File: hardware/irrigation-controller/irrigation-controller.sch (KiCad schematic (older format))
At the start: 80 parts, among them J1 RS485, J10 I2C_2, J11 IO, J12 RELAY_2, J13 RELAY_3B, J14 RELAY_4B, J15 FLOW, J2 I2C_1, J3 ATMEGA ICSP, J4 ATMEGA UART, J5 RF Module, J6 PWR, J7 RELAY_1, J8 RELAY_3A, J9 RELAY_4A, K1 UA2-5NU, K2 UA2-5NU, Q1 MMBT3904, Q2 MMBT3904, Q3 2N7002, Q4 2N7002, Q5 2N7002, Q6 2N7002, SW1 SPST, SW2 SPST, U1 AQY280EH, U2 ATmega328P-AU, U3 AQY280EH, U4 TPS54331DR, U5 TPS54331DR, U6 MAX485, Y1 8MHz

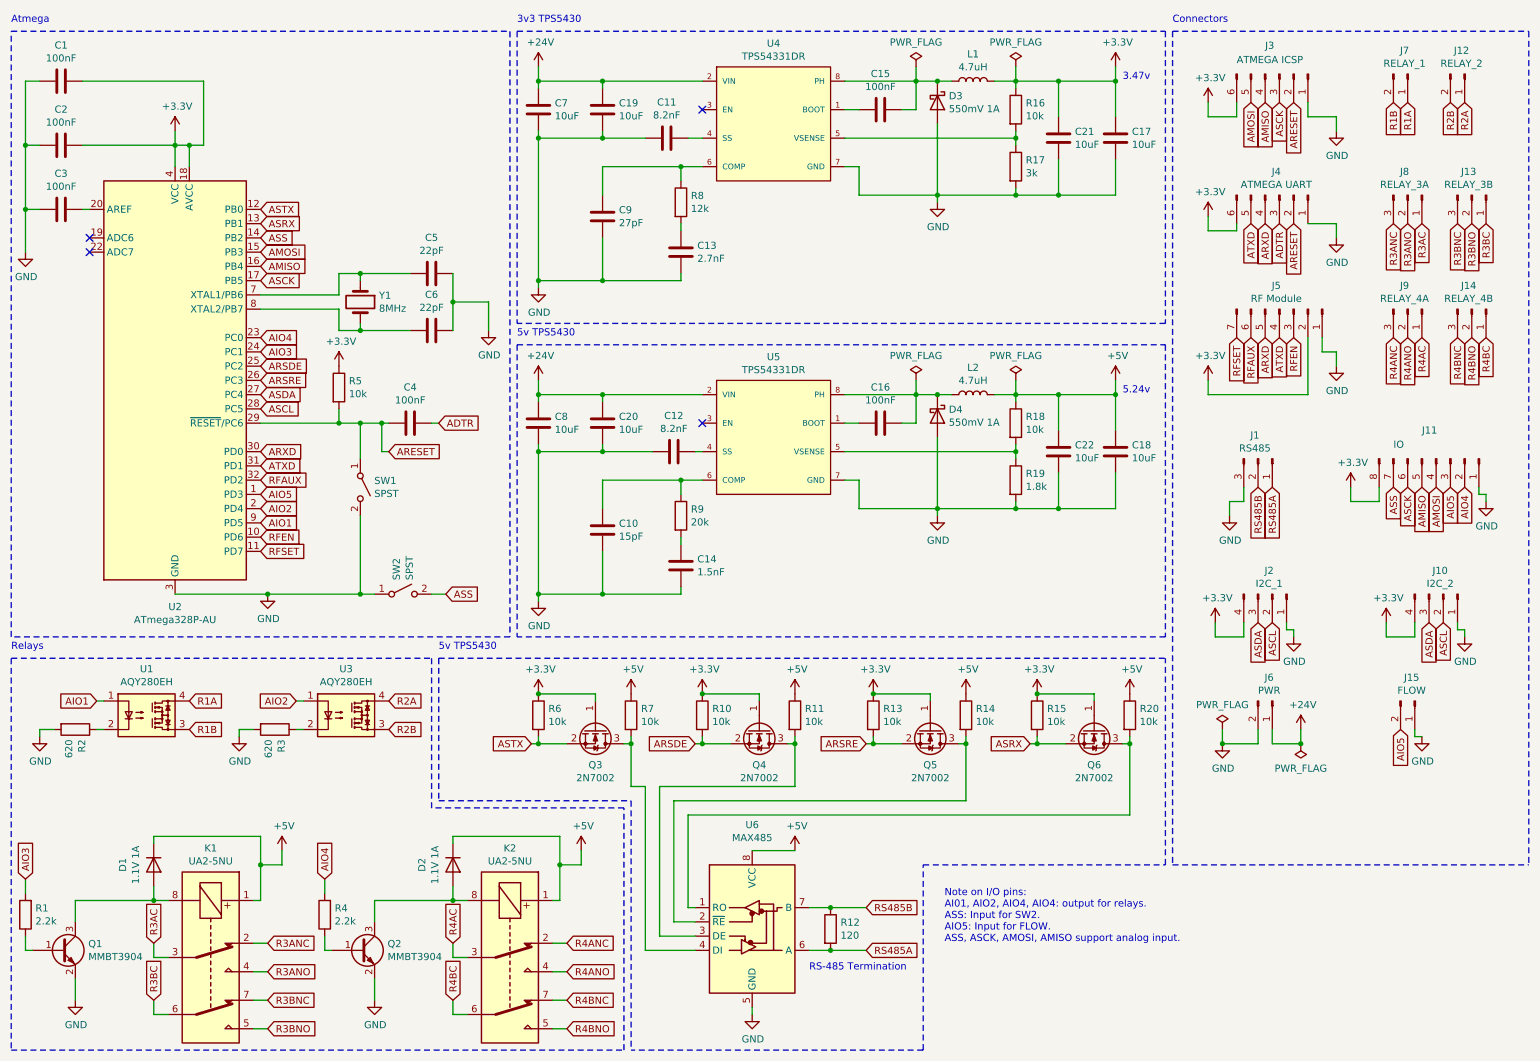
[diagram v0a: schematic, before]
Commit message: Controller board layout wip
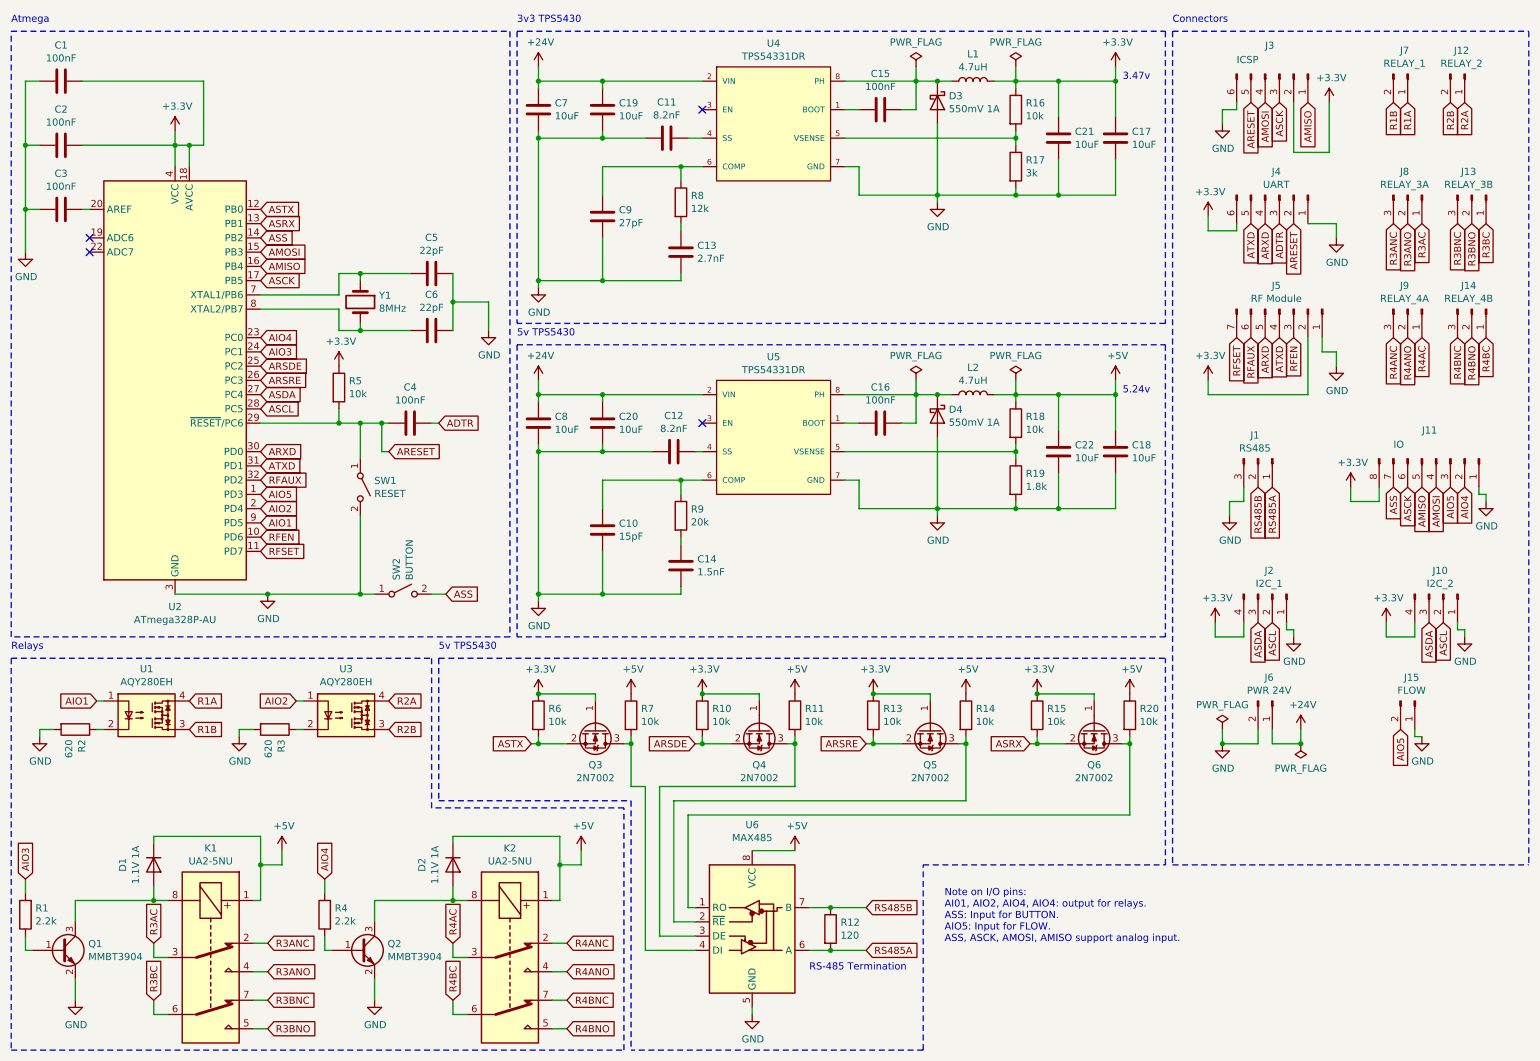
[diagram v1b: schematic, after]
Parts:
- J3: value ATMEGA ICSP -> ICSP
- J4: value ATMEGA UART -> UART
- J6: value PWR -> PWR 24V
- SW1: value SPST -> RESET
- SW2: value SPST -> BUTTON
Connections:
- net +3V3: now also J3.2 (Pin_2); no longer J3.6 (Pin_6)
- net AMISO: now also J3.1 (Pin_1); no longer J3.4 (Pin_4)
- net AMOSI: now also J3.4 (Pin_4); no longer J3.5 (Pin_5)
- net ARESET: now also J3.5 (Pin_5); no longer J3.2 (Pin_2)
- net GND: now also J3.6 (Pin_6); no longer J3.1 (Pin_1)
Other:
- note added: "Note on I/O pins:\nAI01, AIO2, AIO4, AIO4: output for relays.\nASS: Input for BUTTON.\nAIO5: Input for FLOW.\nASS, ASCK, AMOSI, AMISO support analog input."
- note removed: "Note on I/O pins:\nAI01, AIO2, AIO4, AIO4: output for relays.\nASS: Input for SW2.\nAIO5: Input for FLOW.\nASS, ASCK, AMOSI, AMISO support analog input."
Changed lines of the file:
@@
 P 2950 3800
 F 0 "SW1" V 2904 3898 50  0000 L CNN
-F 1 "SPST" V 2995 3898 50  0000 L CNN
+F 1 "RESET" V 2995 3898 50  0000 L CNN
 F 2 "lib:SW_SPST_THT_5.0mm" H 2950 3800 50  0001 C CNN
 F 3 "https://www.farnell.com/datasheets/3176355.pdf" H 2950 3800 50  0001 C CNN
@@
 Wire Wire Line
 	9600 3150 8900 3150
-Text GLabel 9200 1100 3    50   Input ~ 0
+Text GLabel 9300 1100 3    50   Input ~ 0
 AMOSI
-Text GLabel 9300 1100 3    50   Input ~ 0
+Text GLabel 9600 1100 3    50   Input ~ 0
 AMISO
 Text GLabel 9400 1100 3    50   Input ~ 0
@@
 Text GLabel 9200 1950 3    50   Input ~ 0
 ATXD
-Text GLabel 9500 1100 3    50   Input ~ 0
+Text GLabel 9200 1100 3    50   Input ~ 0
 ARESET
 $Comp
 L power:+3.3V #PWR030
 U 1 1 61384461
-P 8900 1100
-F 0 "#PWR030" H 8900 950 50  0001 C CNN
-F 1 "+3.3V" H 8915 1273 50  0000 C CNN
-F 2 "" H 8900 1100 50  0001 C CNN
-F 3 "" H 8900 1100 50  0001 C CNN
-	1    8900 1100
-	1    0    0    -1
-$EndComp
-Wire Wire Line
-	8900 1200 9100 1200
-Wire Wire Line
-	9100 1200 9100 1100
-Wire Wire Line
-	9600 1200 9600 1100
+P 9750 1100
+F 0 "#PWR030" H 9750 950 50  0001 C CNN
+F 1 "+3.3V" H 9765 1273 50  0000 C CNN
+F 2 "" H 9750 1100 50  0001 C CNN
+F 3 "" H 9750 1100 50  0001 C CNN
+	1    9750 1100
+	1    0    0    -1
+$EndComp
 Text GLabel 9400 1950 3    50   Input ~ 0
 ADTR
@@
 P 9400 900
 F 0 "J3" V 9200 800 50  0000 L CNN
-F 1 "ATMEGA ICSP" V 9300 600 50  0000 L CNN
+F 1 "ICSP" V 9300 600 50  0000 L CNN
 F 2 "Connector_PinHeader_2.54mm:PinHeader_2x03_P2.54mm_Vertical" H 9400 900 50  0001 C CNN
 F 3 "~" H 9400 900 50  0001 C CNN
@@
 P 9400 1750
 F 0 "J4" V 9235 1728 50  0000 C CNN
-F 1 "ATMEGA UART" V 9326 1728 50  0000 C CNN
+F 1 "UART" V 9326 1728 50  0000 C CNN
 F 2 "Connector_PinHeader_2.54mm:PinHeader_2x03_P2.54mm_Vertical" H 9400 1750 50  0001 C CNN
 F 3 "~" H 9400 1750 50  0001 C CNN
@@
 Wire Wire Line
 	9100 2000 9100 1950
-Wire Wire Line
-	9800 1200 9600 1200
 Wire Wire Line
 	9600 1950 9800 1950
@@
 L power:GND #PWR037
 U 1 1 614A3FA6
-P 9800 1300
-F 0 "#PWR037" H 9800 1050 50  0001 C CNN
-F 1 "GND" H 9805 1127 50  0000 C CNN
-F 2 "" H 9800 1300 50  0001 C CNN
-F 3 "" H 9800 1300 50  0001 C CNN
-	1    9800 1300
-	1    0    0    -1
-$EndComp
-Wire Wire Line
-	9800 1200 9800 1300
+P 9000 1250
+F 0 "#PWR037" H 9000 1000 50  0001 C CNN
+F 1 "GND" H 9005 1077 50  0000 C CNN
+F 2 "" H 9000 1250 50  0001 C CNN
+F 3 "" H 9000 1250 50  0001 C CNN
+	1    9000 1250
+	1    0    0    -1
+$EndComp
 Wire Wire Line
 	9800 1950 9800 2050
@@
 Wire Wire Line
 	8900 2000 8900 1900
-Wire Wire Line
-	8900 1100 8900 1200
 $Comp
 L Connector:Conn_01x03_Male J1
@@
 $EndComp
 Text Notes 7050 7000 0    50   ~ 0
-Note on I/O pins:\nAI01, AIO2, AIO4, AIO4: output for relays.\nASS: Input for SW2.\nAIO5: Input for FLOW.\nASS, ASCK, AMOSI, AMISO support analog input.
+Note on I/O pins:\nAI01, AIO2, AIO4, AIO4: output for relays.\nASS: Input for BUTTON.\nAIO5: Input for FLOW.\nASS, ASCK, AMOSI, AMISO support analog input.
 Text GLabel 10450 4750 3    50   Input ~ 0
 ASDA
@@
 P 9350 5300
 F 0 "J6" V 9185 5278 50  0000 C CNN
-F 1 "PWR" V 9276 5278 50  0000 C CNN
+F 1 "PWR 24V" V 9276 5278 50  0000 C CNN
 F 2 "Connector_JST:JST_XH_B2B-XH-A_1x02_P2.50mm_Vertical" H 9350 5300 50  0001 C CNN
 F 3 "~" H 9350 5300 50  0001 C CNN
@@
 P 3250 4550
 F 0 "SW2" V 3204 4648 50  0000 L CNN
-F 1 "SPST" V 3295 4648 50  0000 L CNN
+F 1 "BUTTON" V 3295 4648 50  0000 L CNN
 F 2 "lib:SW_SPST_THT_5.0mm" H 3250 4550 50  0001 C CNN
 F 3 "https://www.farnell.com/datasheets/3176355.pdf" H 3250 4550 50  0001 C CNN
@@
 Wire Wire Line
 	10350 5550 10350 5500
+Wire Wire Line
+	9500 1100 9500 1450
+Wire Wire Line
+	9500 1450 9750 1450
+Wire Wire Line
+	9750 1450 9750 1100
+Wire Wire Line
+	9000 1250 9000 1150
+Wire Wire Line
+	9000 1150 9100 1150
+Wire Wire Line
+	9100 1150 9100 1100
 $EndSCHEMATC

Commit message: Controller pcb layout mostly complete
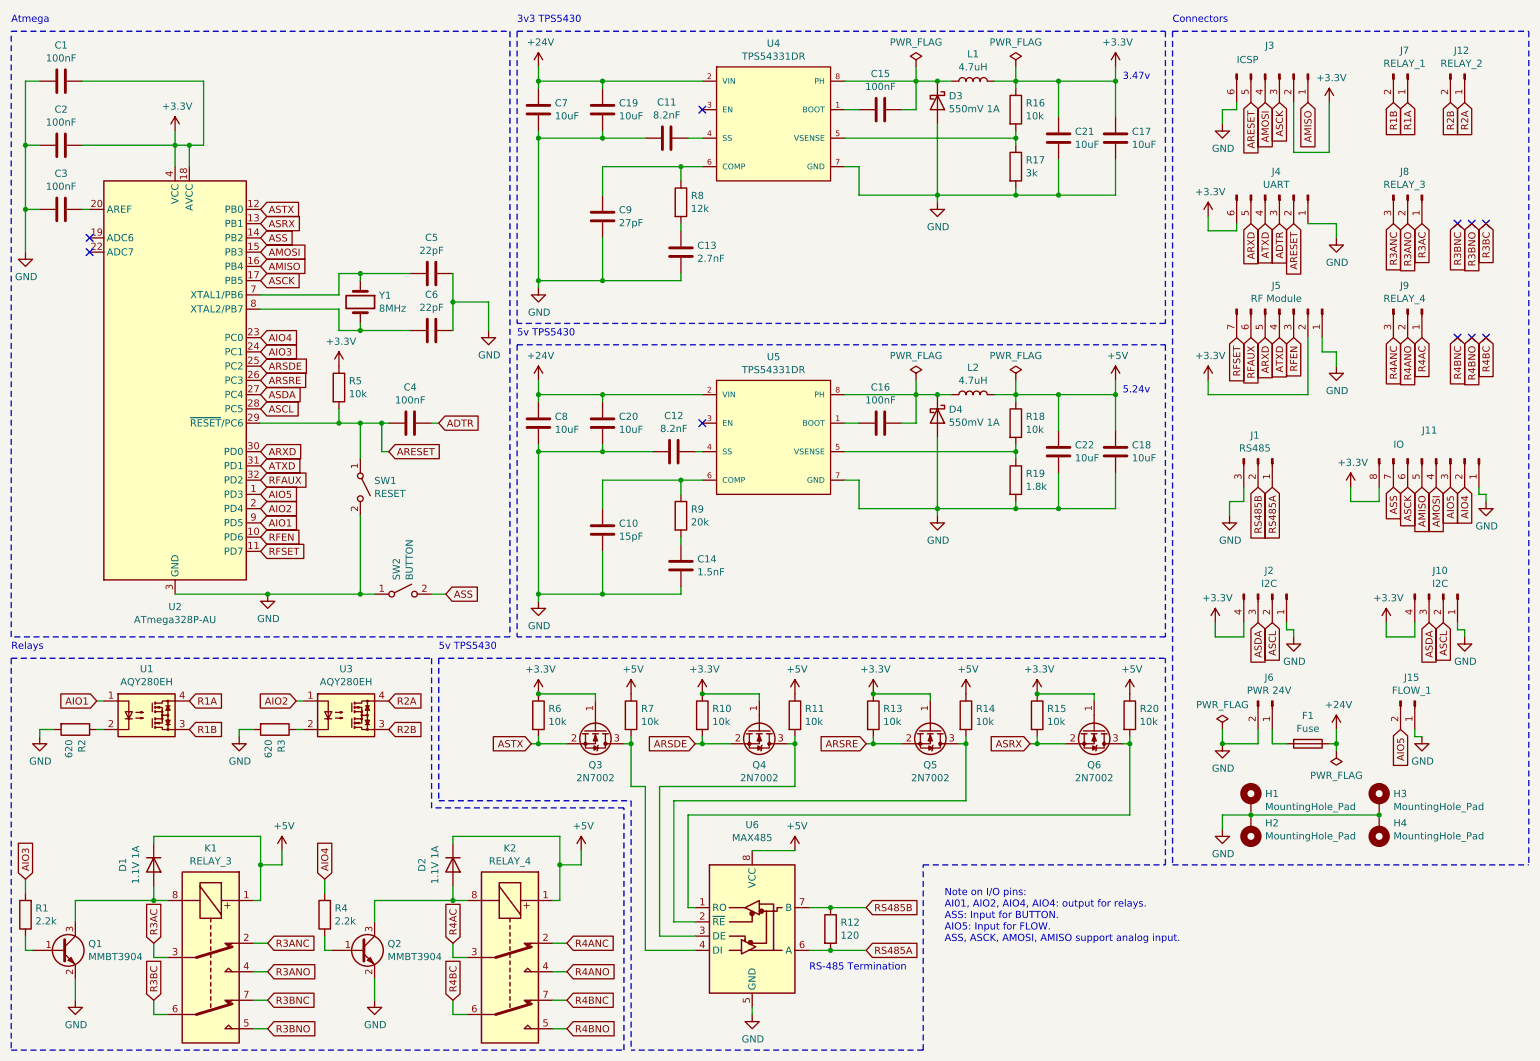
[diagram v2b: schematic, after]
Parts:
- removed J13: RELAY_3B, Connector_JST:JST_XH_B3B-XH-A_1x03_P2.50mm_Vertical, symbol Connector:Conn_01x03_Male
- removed J14: RELAY_4B, Connector_JST:JST_XH_B3B-XH-A_1x03_P2.50mm_Vertical, symbol Connector:Conn_01x03_Male
- added F1: Fuse, Inductor_THT:L_Radial_D8.7mm_P5.00mm_Fastron_07HCP, symbol Device:Fuse
- added H1, H2, H3, H4: MountingHole_Pad, MountingHole:MountingHole_3mm_Pad, symbol Mechanical:MountingHole_Pad
- J10: value I2C_2 -> I2C
- J15: value FLOW -> FLOW_1
- J2: value I2C_1 -> I2C
- J8: value RELAY_3A -> RELAY_3
- J9: value RELAY_4A -> RELAY_4
- K1: value UA2-5NU -> RELAY_3
- K2: value UA2-5NU -> RELAY_4
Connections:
- net +24V: now also F1.1; no longer J6.1 (Pin_1)
- net ARXD: now also J4.5 (Pin_5); no longer J4.4 (Pin_4)
- net ATXD: now also J4.4 (Pin_4); no longer J4.5 (Pin_5)
- net GND: now also H1.1, H2.1, H3.1, H4.1
- new net: F1.2, J6.1 (Pin_1)
- no-connect marks 4 -> 10
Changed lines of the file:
@@
 P 1900 7100
 F 0 "K1" V 1133 7100 50  0000 C CNN
-F 1 "UA2-5NU" V 1224 7100 50  0000 C CNN
+F 1 "RELAY_3" V 1224 7100 50  0000 C CNN
 F 2 "lib:Relay_DPDT_NEXEM_UA2_Pitch3.2mm" H 1900 7100 50  0001 C CNN
 F 3 "https://www.farnell.com/datasheets/2302216.pdf" H 1900 7100 50  0001 C CNN
@@
 P 10300 1750
 F 0 "J8" V 10135 1728 50  0000 C CNN
-F 1 "RELAY_3A" V 10226 1728 50  0000 C CNN
+F 1 "RELAY_3" V 10226 1728 50  0000 C CNN
 F 2 "Connector_JST:JST_XH_B3B-XH-A_1x03_P2.50mm_Vertical" H 10300 1750 50  0001 C CNN
 F 3 "~" H 10300 1750 50  0001 C CNN
 F 4 "https://au.mouser.com/ProductDetail/426-FIT0255" V 10300 1750 50  0001 C CNN "Purchase Link"
 	1    10300 1750
-	0    1    1    0
-$EndComp
-$Comp
-L Connector:Conn_01x03_Male J13
-U 1 1 6142E79F
-P 10750 1750
-F 0 "J13" V 10585 1728 50  0000 C CNN
-F 1 "RELAY_3B" V 10676 1728 50  0000 C CNN
-F 2 "Connector_JST:JST_XH_B3B-XH-A_1x03_P2.50mm_Vertical" H 10750 1750 50  0001 C CNN
-F 3 "~" H 10750 1750 50  0001 C CNN
-F 4 "https://au.mouser.com/ProductDetail/426-FIT0255" V 10750 1750 50  0001 C CNN "Purchase Link"
-	1    10750 1750
 	0    1    1    0
 $EndComp
@@
 Text GLabel 9400 1100 3    50   Input ~ 0
 ASCK
+Text GLabel 9200 1950 3    50   Input ~ 0
+ARXD
 Text GLabel 9300 1950 3    50   Input ~ 0
-ARXD
-Text GLabel 9200 1950 3    50   Input ~ 0
 ATXD
 Text GLabel 9200 1100 3    50   Input ~ 0
@@
 P 9350 4550
 F 0 "J2" V 9185 4528 50  0000 C CNN
-F 1 "I2C_1" V 9276 4528 50  0000 C CNN
+F 1 "I2C" V 9276 4528 50  0000 C CNN
 F 2 "Connector_JST:JST_XH_B4B-XH-A_1x04_P2.50mm_Vertical" H 9350 4550 50  0001 C CNN
 F 3 "~" H 9350 4550 50  0001 C CNN
@@
 P 4000 7100
 F 0 "K2" V 3233 7100 50  0000 C CNN
-F 1 "UA2-5NU" V 3324 7100 50  0000 C CNN
+F 1 "RELAY_4" V 3324 7100 50  0000 C CNN
 F 2 "lib:Relay_DPDT_NEXEM_UA2_Pitch3.2mm" H 4000 7100 50  0001 C CNN
 F 3 "https://www.farnell.com/datasheets/2302216.pdf" H 4000 7100 50  0001 C CNN
@@
 P 10300 2550
 F 0 "J9" V 10135 2528 50  0000 C CNN
-F 1 "RELAY_4A" V 10226 2528 50  0000 C CNN
+F 1 "RELAY_4" V 10226 2528 50  0000 C CNN
 F 2 "Connector_JST:JST_XH_B3B-XH-A_1x03_P2.50mm_Vertical" H 10300 2550 50  0001 C CNN
 F 3 "~" H 10300 2550 50  0001 C CNN
 F 4 "https://au.mouser.com/ProductDetail/426-FIT0255" V 10300 2550 50  0001 C CNN "Purchase Link"
 	1    10300 2550
-	0    1    1    0
-$EndComp
-$Comp
-L Connector:Conn_01x03_Male J14
-U 1 1 6170C928
-P 10750 2550
-F 0 "J14" V 10585 2528 50  0000 C CNN
-F 1 "RELAY_4B" V 10676 2528 50  0000 C CNN
-F 2 "Connector_JST:JST_XH_B3B-XH-A_1x03_P2.50mm_Vertical" H 10750 2550 50  0001 C CNN
-F 3 "~" H 10750 2550 50  0001 C CNN
-F 4 "https://au.mouser.com/ProductDetail/426-FIT0255" V 10750 2550 50  0001 C CNN "Purchase Link"
-	1    10750 2550
 	0    1    1    0
 $EndComp
@@
 P 10550 4550
 F 0 "J10" V 10385 4528 50  0000 C CNN
-F 1 "I2C_2" V 10476 4528 50  0000 C CNN
+F 1 "I2C" V 10476 4528 50  0000 C CNN
 F 2 "Connector_JST:JST_XH_B4B-XH-A_1x04_P2.50mm_Vertical" H 10550 4550 50  0001 C CNN
 F 3 "~" H 10550 4550 50  0001 C CNN
@@
 L power:PWR_FLAG #FLG04
 U 1 1 61923EF8
-P 9550 5600
-F 0 "#FLG04" H 9550 5675 50  0001 C CNN
-F 1 "PWR_FLAG" H 9550 5773 50  0000 C CNN
-F 2 "" H 9550 5600 50  0001 C CNN
-F 3 "~" H 9550 5600 50  0001 C CNN
-	1    9550 5600
+P 9800 5650
+F 0 "#FLG04" H 9800 5725 50  0001 C CNN
+F 1 "PWR_FLAG" H 9800 5823 50  0000 C CNN
+F 2 "" H 9800 5650 50  0001 C CNN
+F 3 "~" H 9800 5650 50  0001 C CNN
+	1    9800 5650
 	-1   0    0    1
 $EndComp
@@
 L power:+24V #PWR041
 U 1 1 61924F74
-P 9550 5500
-F 0 "#PWR041" H 9550 5350 50  0001 C CNN
-F 1 "+24V" H 9565 5673 50  0000 C CNN
-F 2 "" H 9550 5500 50  0001 C CNN
-F 3 "" H 9550 5500 50  0001 C CNN
-	1    9550 5500
+P 9800 5500
+F 0 "#PWR041" H 9800 5350 50  0001 C CNN
+F 1 "+24V" H 9815 5673 50  0000 C CNN
+F 2 "" H 9800 5500 50  0001 C CNN
+F 3 "" H 9800 5500 50  0001 C CNN
+	1    9800 5500
 	1    0    0    -1
 $EndComp
@@
 Wire Wire Line
 	9350 5500 9350 5600
-Wire Wire Line
-	9350 5600 9550 5600
-Wire Wire Line
-	9550 5600 9550 5500
-Connection ~ 9550 5600
 $Comp
 L power:GND #PWR035
@@
 P 10350 5300
 F 0 "J15" V 10185 5278 50  0000 C CNN
-F 1 "FLOW" V 10276 5278 50  0000 C CNN
+F 1 "FLOW_1" V 10276 5278 50  0000 C CNN
 F 2 "Connector_JST:JST_XH_B2B-XH-A_1x02_P2.50mm_Vertical" H 10350 5300 50  0001 C CNN
 F 3 "~" H 10350 5300 50  0001 C CNN
@@
 Wire Wire Line
 	9100 1150 9100 1100
+NoConn ~ 10650 1950
+NoConn ~ 10750 1950
+NoConn ~ 10850 1950
+NoConn ~ 10650 2750
+NoConn ~ 10750 2750
+NoConn ~ 10850 2750
+$Comp
+L Mechanical:MountingHole_Pad H1
+U 1 1 61A279E9
+P 9200 6000
+F 0 "H1" H 9300 6049 50  0000 L CNN
+F 1 "MountingHole_Pad" H 9300 5958 50  0000 L CNN
+F 2 "MountingHole:MountingHole_3mm_Pad" H 9200 6000 50  0001 C CNN
+F 3 "~" H 9200 6000 50  0001 C CNN
+	1    9200 6000
+	1    0    0    -1
+$EndComp
+$Comp
+L Mechanical:MountingHole_Pad H3
+U 1 1 61A28377
+P 10100 6000
+F 0 "H3" H 10200 6049 50  0000 L CNN
+F 1 "MountingHole_Pad" H 10200 5958 50  0000 L CNN
+F 2 "MountingHole:MountingHole_3mm_Pad" H 10100 6000 50  0001 C CNN
+F 3 "~" H 10100 6000 50  0001 C CNN
+	1    10100 6000
+	1    0    0    -1
+$EndComp
+$Comp
+L Mechanical:MountingHole_Pad H2
+U 1 1 61A289B4
+P 9200 6200
+F 0 "H2" H 9100 6157 50  0000 R CNN
+F 1 "MountingHole_Pad" H 9100 6248 50  0000 R CNN
+F 2 "MountingHole:MountingHole_3mm_Pad" H 9200 6200 50  0001 C CNN
+F 3 "~" H 9200 6200 50  0001 C CNN
+	1    9200 6200
+	-1   0    0    1
+$EndComp
+$Comp
+L Mechanical:MountingHole_Pad H4
+U 1 1 61A292A3
+P 10100 6200
+F 0 "H4" H 10000 6157 50  0000 R CNN
+F 1 "MountingHole_Pad" H 10000 6248 50  0000 R CNN
+F 2 "MountingHole:MountingHole_3mm_Pad" H 10100 6200 50  0001 C CNN
+F 3 "~" H 10100 6200 50  0001 C CNN
+	1    10100 6200
+	-1   0    0    1
+$EndComp
+$Comp
+L power:GND #PWR045
+U 1 1 61A29698
+P 9000 6200
+F 0 "#PWR045" H 9000 5950 50  0001 C CNN
+F 1 "GND" H 9005 6027 50  0000 C CNN
+F 2 "" H 9000 6200 50  0001 C CNN
+F 3 "" H 9000 6200 50  0001 C CNN
+	1    9000 6200
+	1    0    0    -1
+$EndComp
+Wire Wire Line
+	9000 6200 9000 6100
+Wire Wire Line
+	9000 6100 9200 6100
+Connection ~ 9200 6100
+Wire Wire Line
+	9200 6100 10100 6100
+Connection ~ 10100 6100
+$Comp
+L Device:Fuse F1
+U 1 1 61A87884
+P 9600 5600
+F 0 "F1" V 9403 5600 50  0000 C CNN
+F 1 "Fuse" V 9494 5600 50  0000 C CNN
+F 2 "Inductor_THT:L_Radial_D8.7mm_P5.00mm_Fastron_07HCP" V 9530 5600 50  0001 C CNN
+F 3 "~" H 9600 5600 50  0001 C CNN
+F 4 "https://au.mouser.com/ProductDetail/530-MRF200" H 9600 5600 50  0001 C CNN "Purchase Link"
+	1    9600 5600
+	0    1    1    0
+$EndComp
+Wire Wire Line
+	9800 5500 9800 5600
+Wire Wire Line
+	9800 5600 9750 5600
+Wire Wire Line
+	9450 5600 9350 5600
+Wire Wire Line
+	9800 5650 9800 5600
+Connection ~ 9800 5600
 $EndSCHEMATC
